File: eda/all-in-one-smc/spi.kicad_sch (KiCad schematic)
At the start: 14 parts, among them U23 74HCT14, U24 74HCT86, U26 74HCT595, U27 74HCT165, U28 74AHCT541, U31 74HCT138

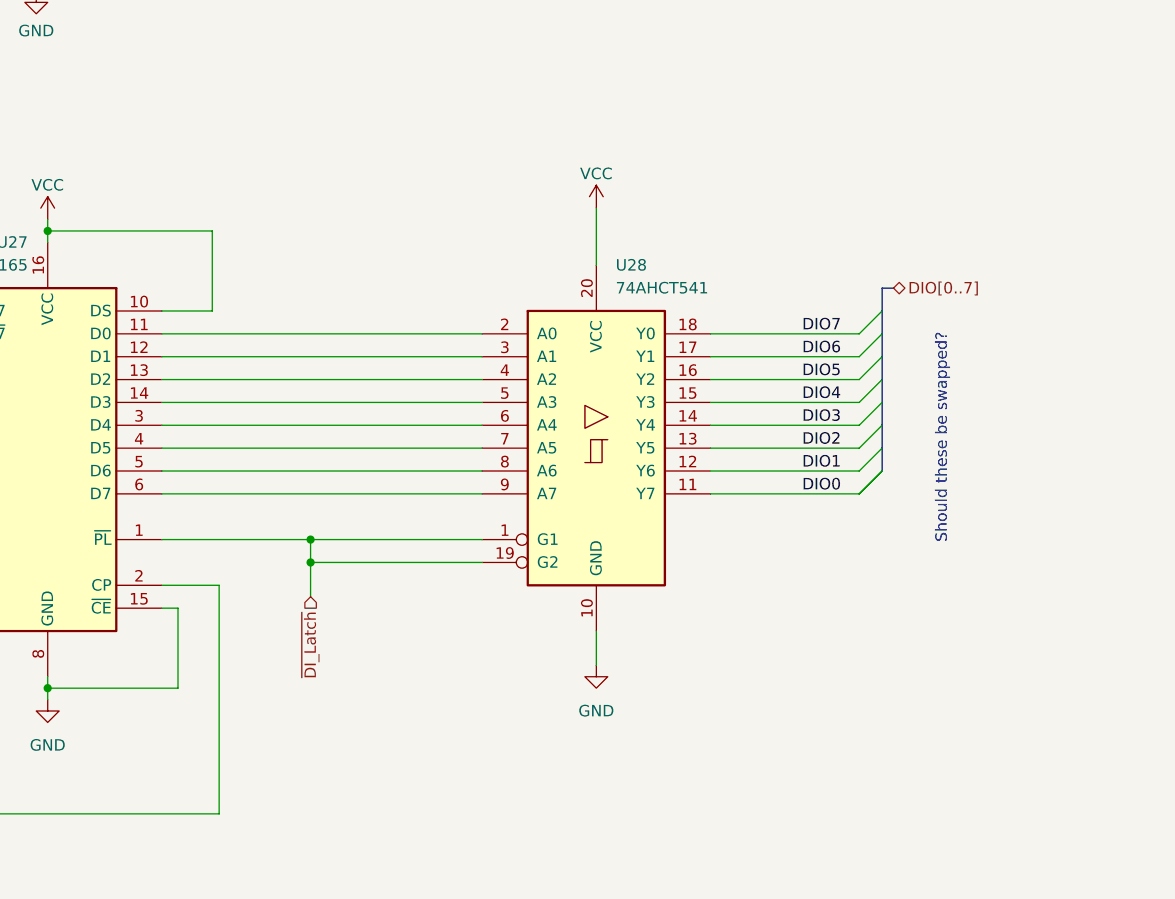
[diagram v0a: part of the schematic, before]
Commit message: WIP: Implementing new SPI and IO card
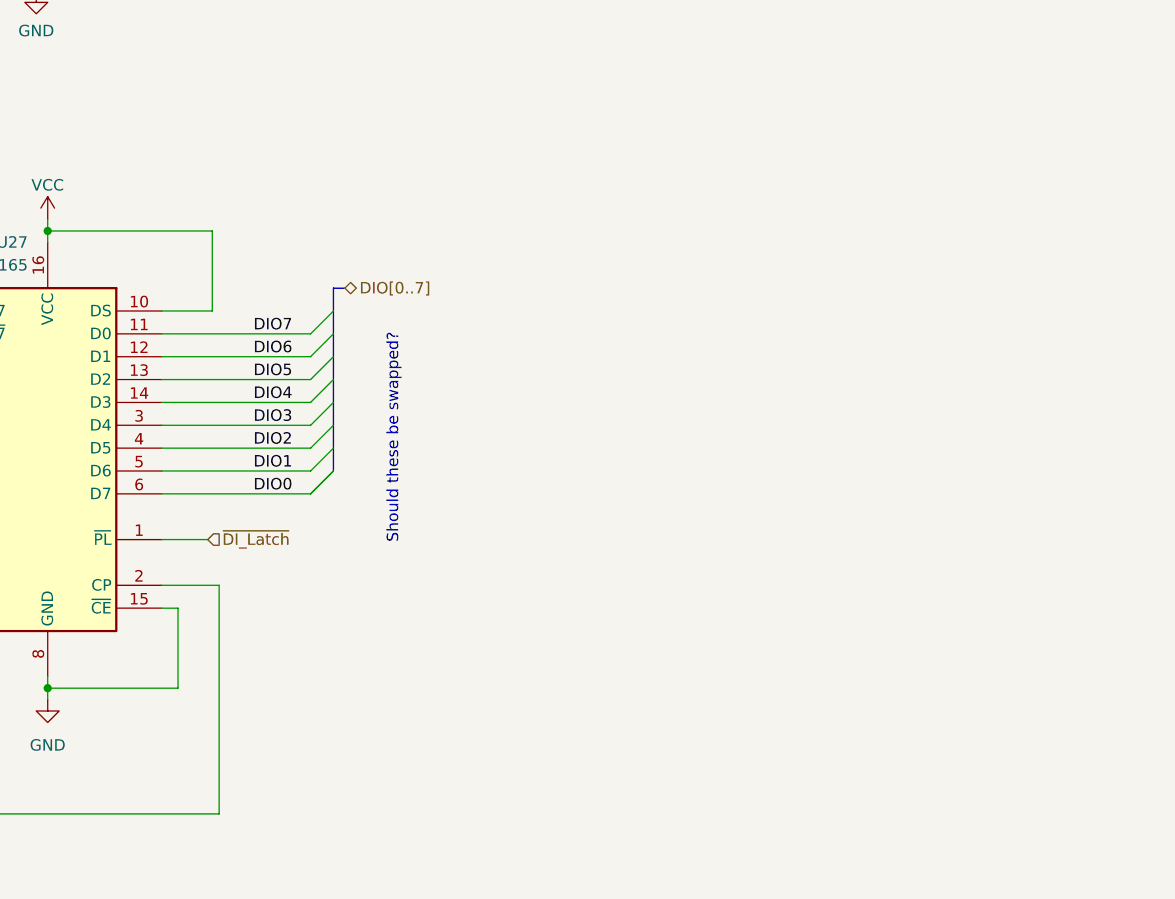
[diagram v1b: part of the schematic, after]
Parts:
- removed U28: 74AHCT541, Package_SO:SOIC-20W_7.5x12.8mm_P1.27mm, symbol 74xx:74AHCT541
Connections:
- net DIO0: now also U27.6 (D7)
- net DIO1: now also U27.5 (D6)
- net DIO2: now also U27.4 (D5)
- net DIO3: now also U27.3 (D4)
- net DIO4: now also U27.14 (D3)
- net DIO5: now also U27.13 (D2)
- net DIO6: now also U27.12 (D1)
- net DIO7: now also U27.11 (D0)

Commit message: wip
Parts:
- removed JP3, JP4, JP5: ~, Connector_PinHeader_2.54mm:PinHeader_1x03_P2.54mm_Vertical, symbol Jumper:Jumper_3_Bridged12
- added J13: CS_Invert_Selection, Connector_PinHeader_2.54mm:PinHeader_2x03_P2.54mm_Horizontal, symbol Connector_Generic:Conn_02x03_Odd_Even
- added R40, R41, R42: 10k, Resistor_SMD:R_0805_2012Metric, symbol Device:R
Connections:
- net GND: now also R40.2, R41.2, R42.2
- net VCC: now also J13.2 (Pin_2), J13.4 (Pin_4), J13.6 (Pin_6)
- net at U24.5: now also J13.5 (Pin_5), R42.1
- net at U24.13: now also J13.1 (Pin_1), R40.1
- net at U24.10: now also J13.3 (Pin_3), R41.1
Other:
- moved on the sheet: U24B, U24C, U24D, U31
